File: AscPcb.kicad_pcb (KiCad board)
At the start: 2 copper layers, 73.4 x 73.8 mm, 64 parts, among them J1 12402012E212A, J2 B2B-PH-K-S(LF)(SN), J3 Conn_01x10_Pin, J4 Conn_01x06_Pin, J5 Screw_Terminal_01x02, J6 Conn_01x02_Pin, J7 Conn_01x02_Pin, J8 Conn_01x03_Pin, J9 Screw_Terminal_01x02, Q1 Q_NMOS_DGS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

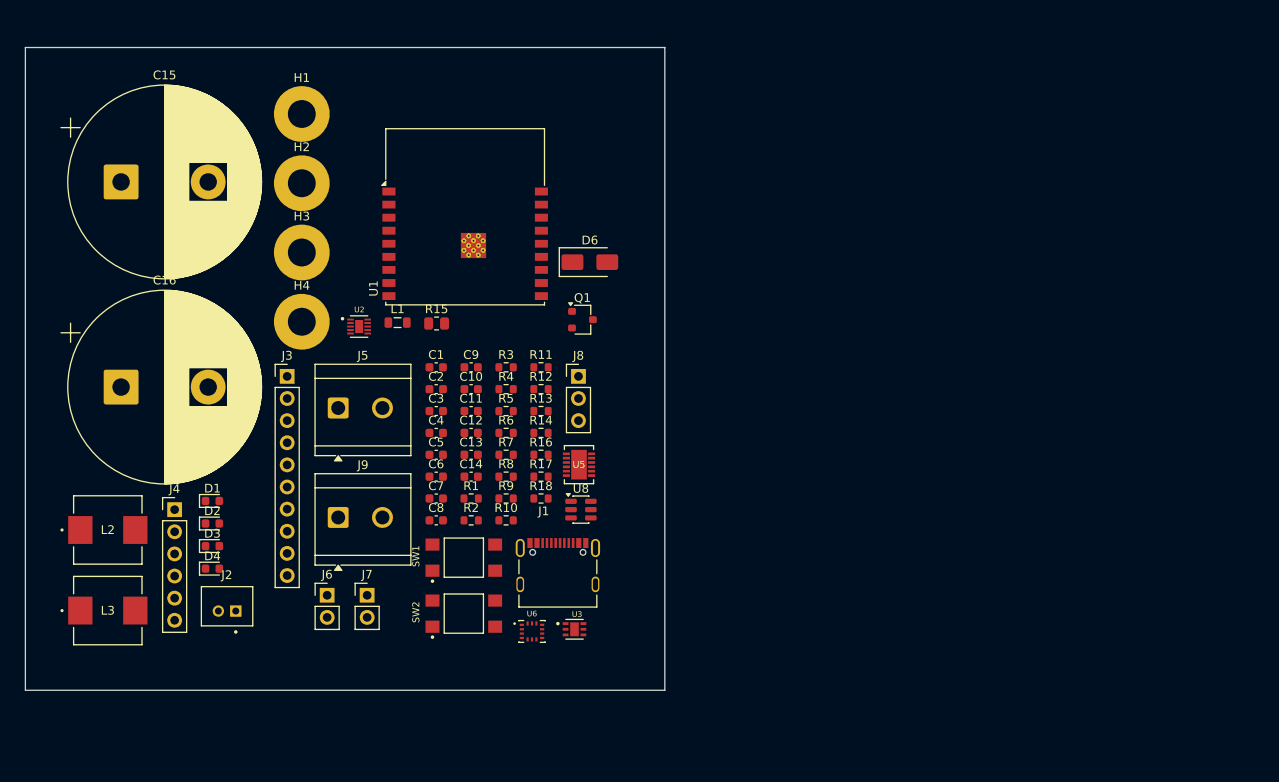
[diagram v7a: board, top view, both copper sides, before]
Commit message: usb to serial converter, some safety features and monitoring
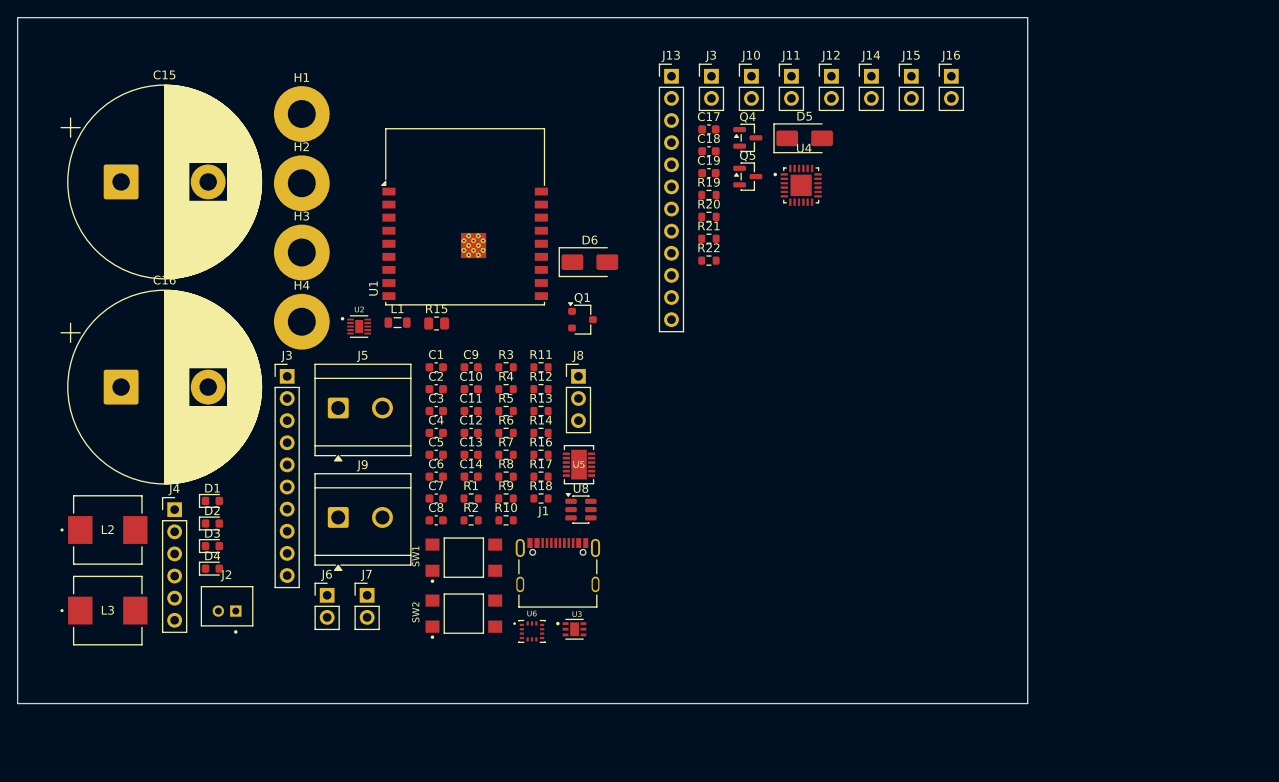
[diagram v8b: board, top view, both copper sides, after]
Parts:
- added C17: 100nF, Capacitor_SMD:C_0603_1608Metric, F.Cu at (175.8, 55.8)
- added C18: 100nF, Capacitor_SMD:C_0603_1608Metric, F.Cu at (175.8, 58.3)
- added C19: 4.7uF, Capacitor_SMD:C_0603_1608Metric, F.Cu at (175.8, 60.8)
- added D5: D_Schottky, Diode_SMD:D_SMA, F.Cu at (186.7, 56.8)
- added J10: Conn_01x02_Pin, Connector_PinHeader_2.54mm:PinHeader_1x02_P2.54mm_Vertical, F.Cu at (180.6, 49.7)
- added J11: Conn_01x02_Pin, Connector_PinHeader_2.54mm:PinHeader_1x02_P2.54mm_Vertical, F.Cu at (185.2, 49.7)
- added J12: Conn_01x02_Pin, Connector_PinHeader_2.54mm:PinHeader_1x02_P2.54mm_Vertical, F.Cu at (189.8, 49.7)
- added J13: Conn_01x12_Pin, Connector_PinHeader_2.54mm:PinHeader_1x12_P2.54mm_Vertical, F.Cu at (171.5, 49.7)
- added J14: Conn_01x02_Pin, Connector_PinHeader_2.54mm:PinHeader_1x02_P2.54mm_Vertical, F.Cu at (194.4, 49.7)
- added J15: Conn_01x02_Pin, Connector_PinHeader_2.54mm:PinHeader_1x02_P2.54mm_Vertical, F.Cu at (199.0, 49.7)
- added J16: Conn_01x02_Pin, Connector_PinHeader_2.54mm:PinHeader_1x02_P2.54mm_Vertical, F.Cu at (203.6, 49.7)
- added J3: Conn_01x02_Pin, Connector_PinHeader_2.54mm:PinHeader_1x02_P2.54mm_Vertical, F.Cu at (176.0, 49.7)
- added Q4: BC817, Package_TO_SOT_SMD:SOT-23, F.Cu at (180.2, 56.7)
- added Q5: BC817, Package_TO_SOT_SMD:SOT-23, F.Cu at (180.2, 61.2)
- added R19: 10k, Resistor_SMD:R_0603_1608Metric, F.Cu at (175.8, 63.3)
- added R20: 10k, Resistor_SMD:R_0603_1608Metric, F.Cu at (175.8, 65.8)
- added R21: 1k, Resistor_SMD:R_0603_1608Metric, F.Cu at (175.8, 68.3)
- added R22: 10k, Resistor_SMD:R_0603_1608Metric, F.Cu at (175.8, 70.8)
- added U4: CP2102N-A02-GQFN24R, CP2102N-A02-GQFN24R:QFN50P400X400X80-25N, F.Cu at (186.3, 62.2)
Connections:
- net Net-(U1-EN) renamed EN
- net Net-(U1-IO9) renamed IO9
- J1 pad A4_B9: +5V -> Net-(D5-A)
- J1 pad B4_A9: +5V -> Net-(D5-A)
- Q1 pad 2: IO3 -> Net-(Q1-G)
- U1 pad 11: IO20 -> ESP_RXD
- U1 pad 12: IO21 -> ESP_TXD
- U1 pad 13: D- -> IO18
- U1 pad 14: D+ -> IO19
- U6 pad 1: SA0 -> GND
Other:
- board size 73.4 x 73.8 mm -> 116 x 78.7 mm
